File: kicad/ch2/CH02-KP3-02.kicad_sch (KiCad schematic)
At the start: 5 parts

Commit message: regular
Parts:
- removed R4: 3, symbol Device:R_US
- removed R5: 5, symbol Device:R_US
- removed V3: 30, symbol Simulation_SPICE:VDC
- removed V4: 10, symbol Simulation_SPICE:VDC
- removed V5: 8, symbol Simulation_SPICE:VDC
- added I1: 3, symbol Simulation_SPICE:IDC
- added R6: 4, symbol Device:R_US
- added R7: 2, symbol Device:R_US
- added R8: 3, symbol Device:R_US
- added R9: 8, symbol Device:R_US
- added V6: 12, symbol Simulation_SPICE:VDC
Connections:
- net 0: now also I1.2, R6.2, R9.2, V6.2
- new net: I1.1, R6.1, R7.1
- new net: R8.2, V6.1
- new net vo: R7.2, R8.1, R9.1

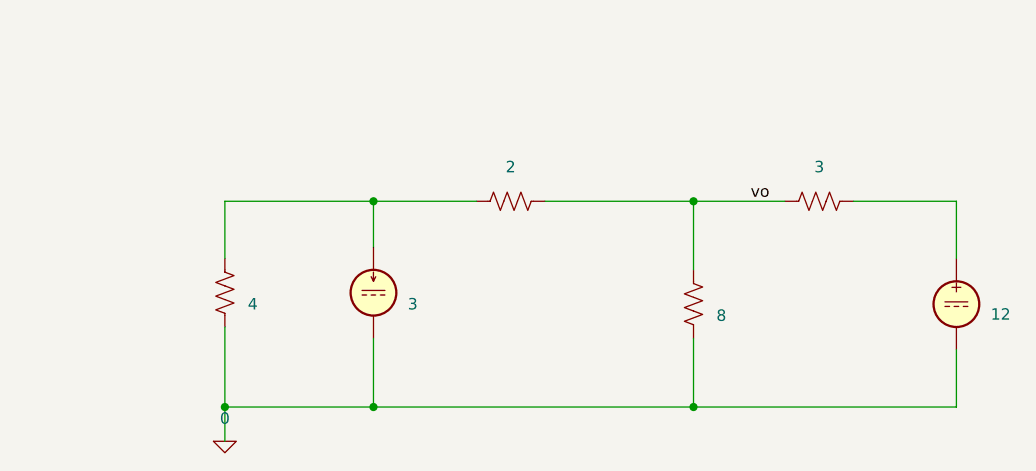
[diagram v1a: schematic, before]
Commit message: fix subsheet sim problem
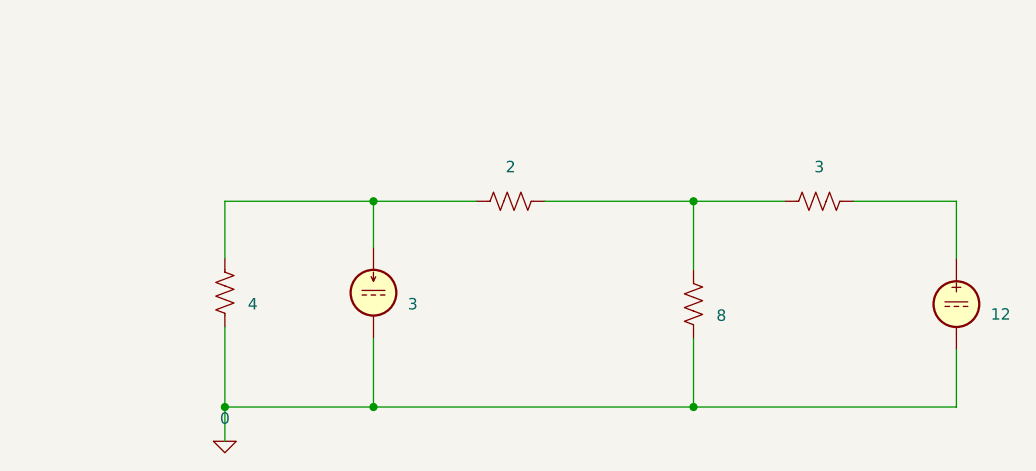
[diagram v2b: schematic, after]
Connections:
- net vo: no longer names the net of R7.2, R8.1, R9.1
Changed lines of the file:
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@@
-		)
-	)
-	(label "vo"
-		(at 135.89 67.31 0)
-		(effects
-			(font
-				(size 1.27 1.27)
-			)
-			(justify left bottom)
 		)
 	)
